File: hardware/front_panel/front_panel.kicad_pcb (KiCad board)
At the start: 2 copper layers, 73 x 54.5 mm, 7 parts

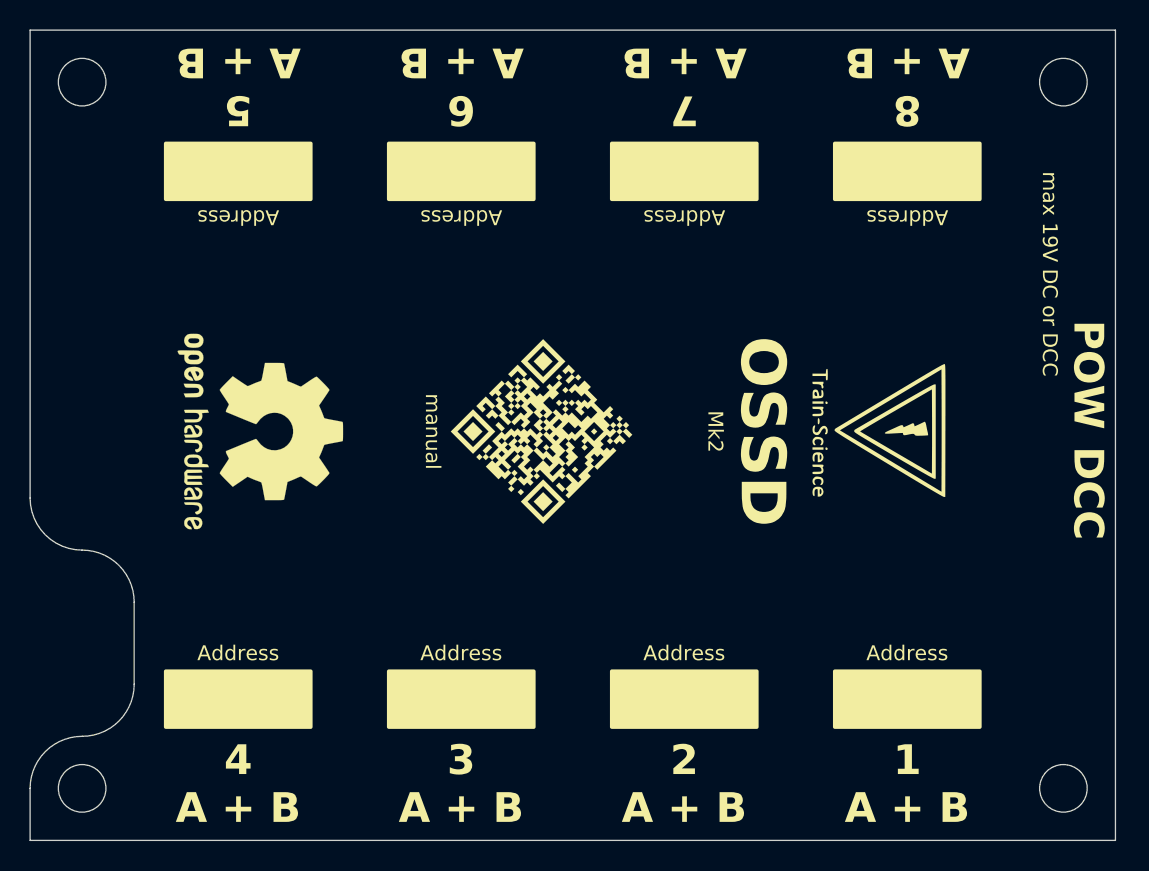
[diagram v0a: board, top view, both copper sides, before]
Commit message: organized board files and added pictures
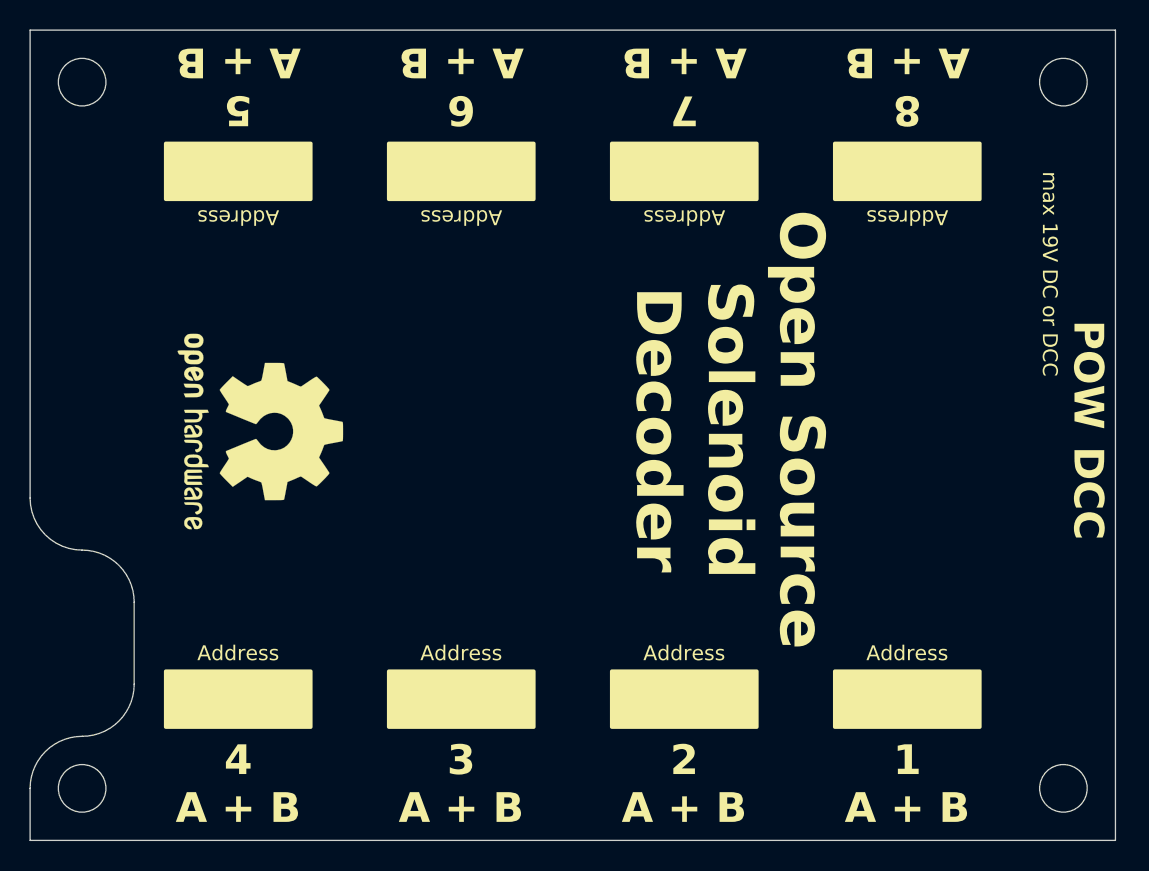
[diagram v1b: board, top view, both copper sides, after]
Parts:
- removed G***: LOGO, custom_kicad_lib_sk:OSSD_QR
- removed G***: LOGO, custom_kicad_lib_sk:Train-Science logo small
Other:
- board text added: "Open Source Solenoid Decoder"
- board text removed: "Mk2"
- board text removed: "OSSD"
- board text removed: "manual"
